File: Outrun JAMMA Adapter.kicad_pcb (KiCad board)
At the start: 2 copper layers, 111 x 86.6 mm, 31 parts, among them U1 LM386, U2 MCP4902, U3 ATMEGA328

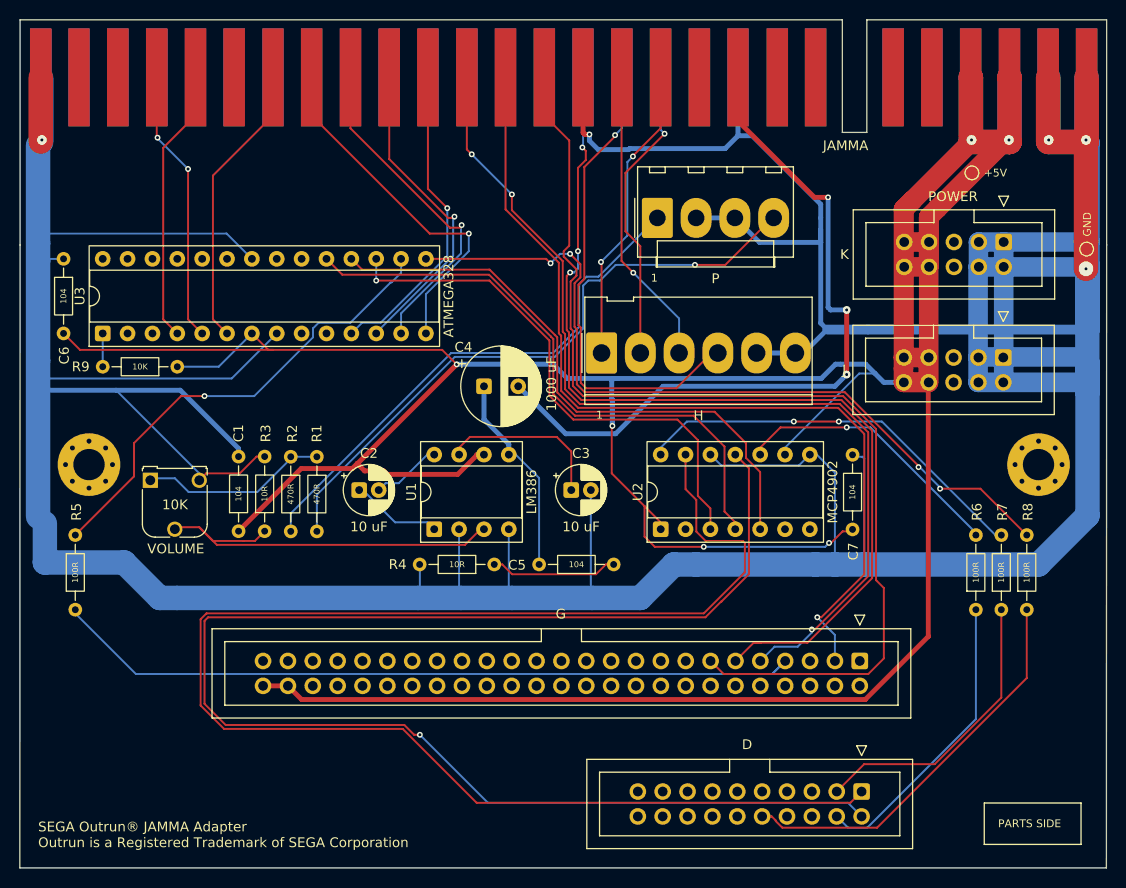
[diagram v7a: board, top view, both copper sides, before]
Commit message: Move bottom ribbon to center to avoid ribbon damage, make connector labels larger
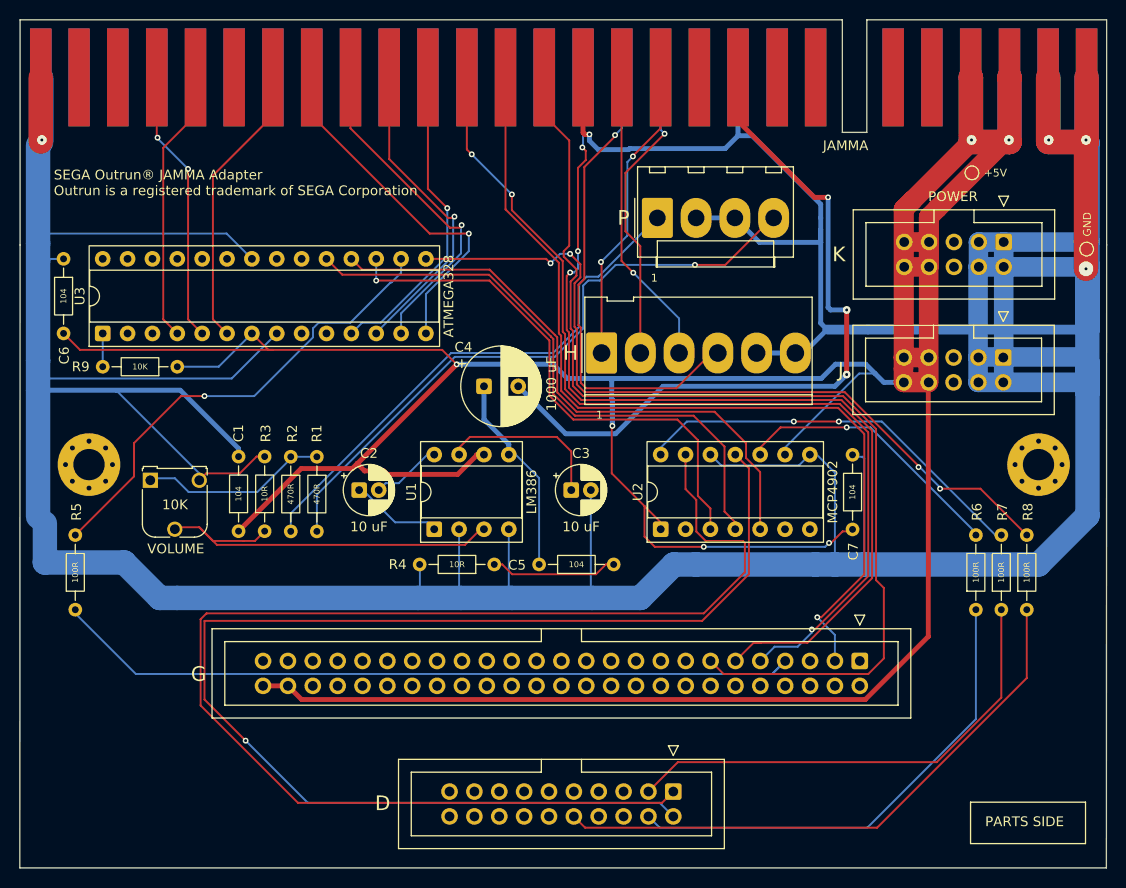
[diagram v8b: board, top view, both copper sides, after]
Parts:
- moved D 19.2 mm to (160.7, 142.2)
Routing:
- net REFA: track 155.6 -> 136.0 mm
- net REFB: track 150.7 -> 131.2 mm
- net STEER: track 30.5 -> 49.7 mm
- net ACCEL: track 29.8 -> 49.0 mm
- net BRK: track 40.9 -> 60.1 mm
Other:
- board text added: "SEGA Outrun® JAMMA Adapter Outrun is a registered trademark of SEGA Corporation"
- board text removed: "SEGA Outrun® JAMMA Adapter Outrun is a Registered Trademark of SEGA Corporation"
